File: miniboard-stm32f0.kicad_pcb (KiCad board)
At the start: 2 copper layers, 39.1 x 19.4 mm, 27 parts, among them P1 CONN_01X02, P2 CONN_01X11, P3 CONN_01X01, P4 CONN_02X03, SW1 SW_PUSH, SW2 SW_PUSH, U1 stm32f030f4p6, Y1 8MHz

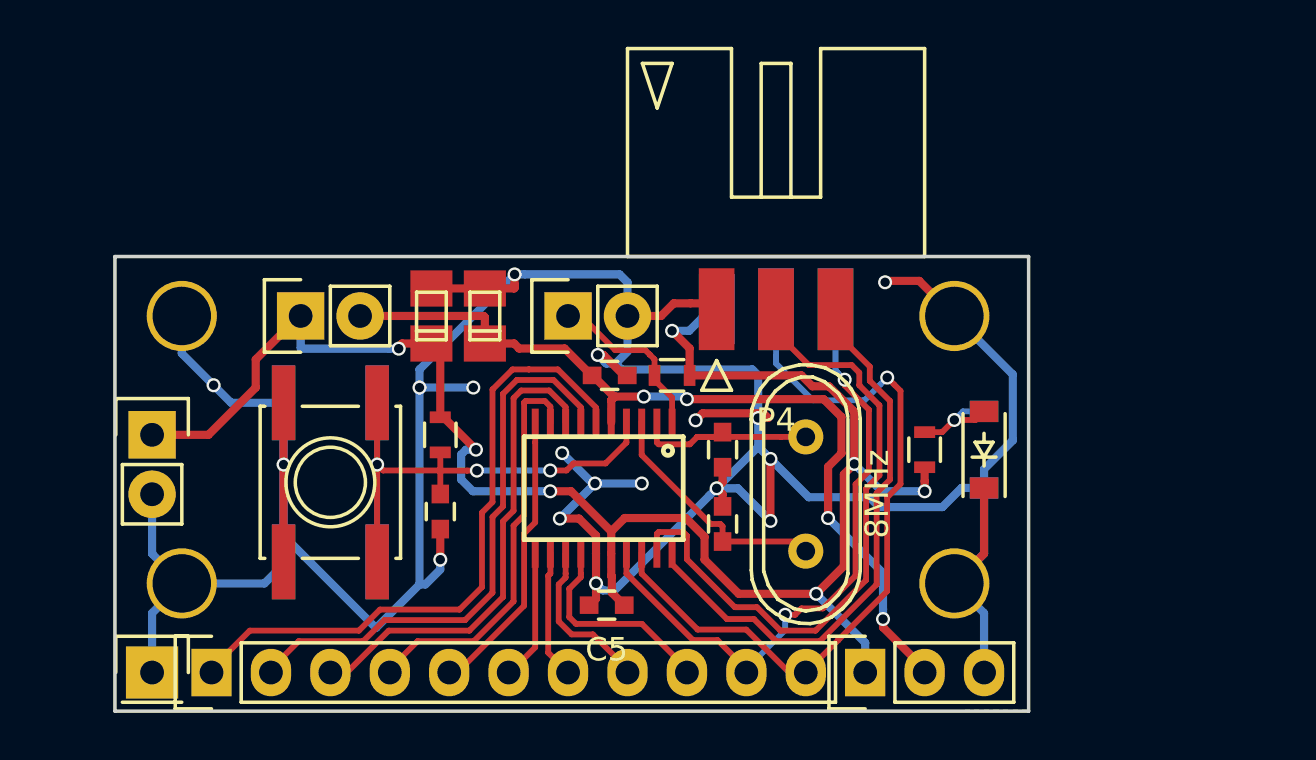
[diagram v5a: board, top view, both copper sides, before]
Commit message: Change direction of power connector
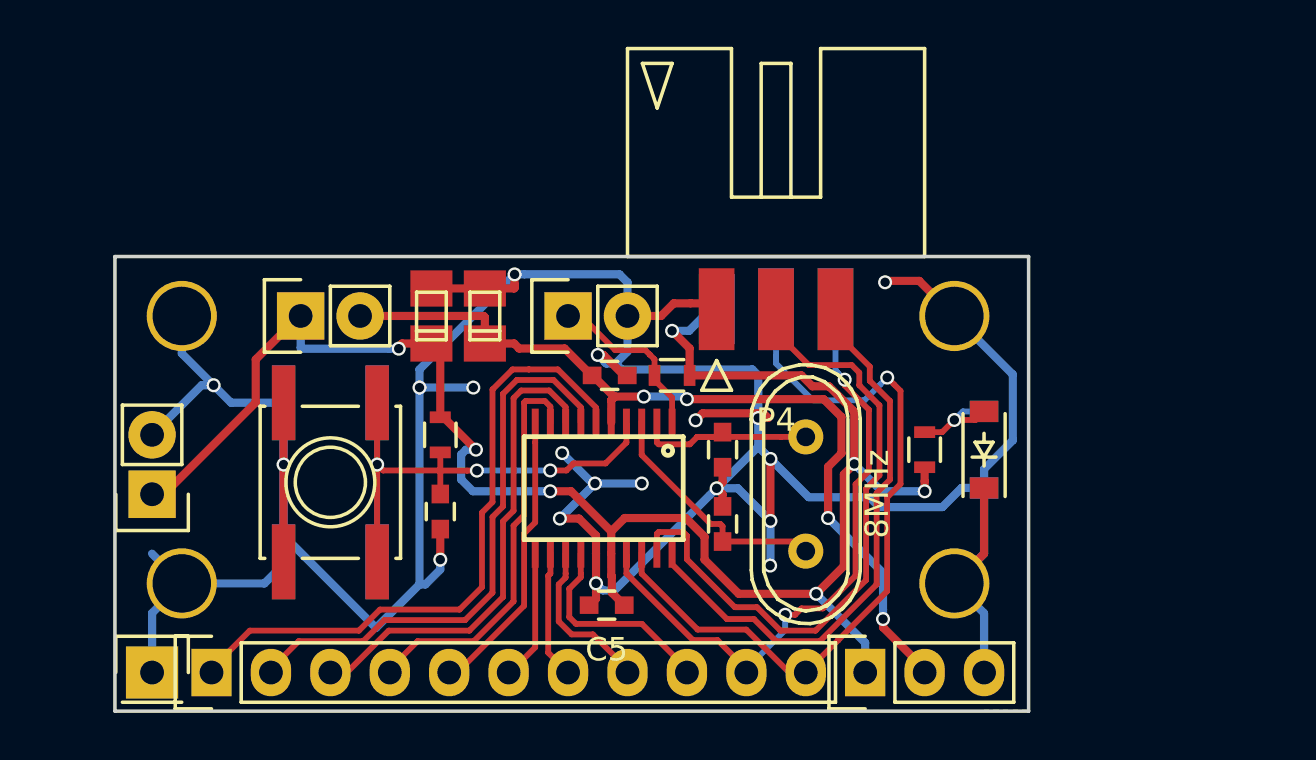
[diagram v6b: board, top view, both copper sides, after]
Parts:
- moved P_POWER1 2.54 mm to (115.6, 111.8), turned to 180 degrees
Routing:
- net GND: track 163.9 -> 166.8 mm, vias 18 -> 19
- net +3V3: track 74.8 -> 76.2 mm
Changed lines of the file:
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@@
     (links 64)
     (no_connects 0)
-    (area 113.907499 101.524999 153.110001 121.106001)
+    (area 110.461667 90.315 154.205 126.393095)
     (thickness 1.6)
-    (drawings 54)
-    (tracks 425)
+    (drawings 57)
+    (tracks 429)
     (zones 0)
     (modules 27)
@@
   )
   (module Pin_Headers:Pin_Header_Straight_1x02 (layer F.Cu)
-    (at 115.57 109.22)
+    (at 115.57 111.76 180)
     (descr "Through hole pin header")
     (tags "pin header")
-    (fp_text reference P_POWER1 (at 0 -5.1) (layer F.SilkS) hide
-      (effects (font (size 1 1) (thickness 0.15)))
-    )
-    (fp_text value CONN_01X02 (at 0 -3.1) (layer F.Fab) hide
+    (fp_text reference P_POWER1 (at 0 -5.1 180) (layer F.SilkS) hide
+      (effects (font (size 1 1) (thickness 0.15)))
+    )
+    (fp_text value CONN_01X02 (at 0 -3.1 180) (layer F.Fab) hide
       (effects (font (size 1 1) (thickness 0.15)))
     )
@@
     (fp_line (start -1.27 1.27) (end -1.27 3.81) (layer F.SilkS) (width 0.15))
     (fp_line (start -1.27 3.81) (end 1.27 3.81) (layer F.SilkS) (width 0.15))
-    (pad 1 thru_hole rect (at 0 0) (size 2.032 2.032) (drill 1.016) (layers *.Cu *.Mask F.SilkS)
+    (pad 1 thru_hole rect (at 0 0 180) (size 2.032 2.032) (drill 1.016) (layers *.Cu *.Mask F.SilkS)
       (net 5 +3V3))
-    (pad 2 thru_hole oval (at 0 2.54) (size 2.032 2.032) (drill 1.016) (layers *.Cu *.Mask F.SilkS)
+    (pad 2 thru_hole oval (at 0 2.54 180) (size 2.032 2.032) (drill 1.016) (layers *.Cu *.Mask F.SilkS)
       (net 2 GND))
     (model Pin_Headers.3dshapes/Pin_Header_Straight_1x02.wrl
@@
       (net 2 GND) (solder_mask_margin 1) (clearance 1))
   )
+  (dimension 50.165 (width 0.3) (layer Dwgs.User)
+    (gr_text "50,165 mm" (at 127.9525 135.335) (layer Dwgs.User)
+      (effects (font (size 1.5 1.5) (thickness 0.3)))
+    )
+    (feature1 (pts (xy 102.87 131.445) (xy 102.87 136.685)))
+    (feature2 (pts (xy 153.035 131.445) (xy 153.035 136.685)))
+    (crossbar (pts (xy 153.035 133.985) (xy 102.87 133.985)))
+    (arrow1a (pts (xy 102.87 133.985) (xy 103.996504 133.398579)))
+    (arrow1b (pts (xy 102.87 133.985) (xy 103.996504 134.571421)))
+    (arrow2a (pts (xy 153.035 133.985) (xy 151.908496 133.398579)))
+    (arrow2b (pts (xy 153.035 133.985) (xy 151.908496 134.571421)))
+  )
+  (dimension 19.685 (width 0.3) (layer Dwgs.User)
+    (gr_text "19,685 mm" (at 160.1 111.4425 90) (layer Dwgs.User)
+      (effects (font (size 1.5 1.5) (thickness 0.3)))
+    )
+    (feature1 (pts (xy 156.21 101.6) (xy 161.45 101.6)))
+    (feature2 (pts (xy 156.21 121.285) (xy 161.45 121.285)))
+    (crossbar (pts (xy 158.75 121.285) (xy 158.75 101.6)))
+    (arrow1a (pts (xy 158.75 101.6) (xy 159.336421 102.726504)))
+    (arrow1b (pts (xy 158.75 101.6) (xy 158.163579 102.726504)))
+    (arrow2a (pts (xy 158.75 121.285) (xy 159.336421 120.158496)))
+    (arrow2b (pts (xy 158.75 121.285) (xy 158.163579 120.158496)))
+  )
+  (dimension 39.37 (width 0.3) (layer Dwgs.User)
+    (gr_text "39,370 mm" (at 133.35 126.445) (layer Dwgs.User)
+      (effects (font (size 1.5 1.5) (thickness 0.3)))
+    )
+    (feature1 (pts (xy 113.665 121.92) (xy 113.665 127.795)))
+    (feature2 (pts (xy 153.035 121.92) (xy 153.035 127.795)))
+    (crossbar (pts (xy 153.035 125.095) (xy 113.665 125.095)))
+    (arrow1a (pts (xy 113.665 125.095) (xy 114.791504 124.508579)))
+    (arrow1b (pts (xy 113.665 125.095) (xy 114.791504 125.681421)))
+    (arrow2a (pts (xy 153.035 125.095) (xy 151.908496 124.508579)))
+    (arrow2b (pts (xy 153.035 125.095) (xy 151.908496 125.681421)))
+  )
   (gr_text RESET (at 127.254 109.22 270) (layer B.SilkS)
     (effects (font (size 1 1) (thickness 0.2)) (justify right mirror))
   )
-  (gr_text SWCLK (at 135.382 109.728 360) (layer B.SilkS)
-    (effects (font (size 1 1) (thickness 0.2)) (justify left mirror))
-  )
-  (gr_text SWDIO (at 135.382 111.76 360) (layer B.SilkS)
-    (effects (font (size 1 1) (thickness 0.2)) (justify left mirror))
-  )
-  (gr_text GND (at 135.382 113.538 360) (layer B.SilkS)
+  (gr_text SWCLK (at 135.382 109.728) (layer B.SilkS)
+    (effects (font (size 1 1) (thickness 0.2)) (justify left mirror))
+  )
+  (gr_text SWDIO (at 135.382 111.76) (layer B.SilkS)
+    (effects (font (size 1 1) (thickness 0.2)) (justify left mirror))
+  )
+  (gr_text GND (at 135.382 113.538) (layer B.SilkS)
     (effects (font (size 1 1) (thickness 0.2)) (justify left mirror))
   )
@@
   (gr_line (start 138.43 114.3) (end 135.636 114.3) (layer B.SilkS) (width 0.2))
   (gr_line (start 138.43 108.966) (end 138.43 114.3) (layer B.SilkS) (width 0.2))
-  (gr_text 3.3 (at 138.684 113.538 360) (layer B.SilkS)
+  (gr_text 3.3 (at 138.684 113.538) (layer B.SilkS)
     (effects (font (size 1 1) (thickness 0.2)) (justify right mirror))
   )
-  (gr_text 3.3V (at 116.84 109.22 360) (layer B.SilkS)
+  (gr_text 3.3V (at 116.84 111.76) (layer B.SilkS)
     (effects (font (size 1 1) (thickness 0.2)) (justify right mirror))
   )
@@
     (effects (font (size 1 1) (thickness 0.2)) (justify right mirror))
   )
-  (gr_text GND (at 118.364 111.76 360) (layer B.SilkS)
+  (gr_text GND (at 118.364 109.22) (layer B.SilkS)
     (effects (font (size 1 1) (thickness 0.2)) (justify mirror))
   )
@@
   (segment (start 137.145 109.55) (end 137.220001 109.625001) (width 0.25) (layer F.Cu) (net 1))
   (segment (start 137.145 108.7) (end 137.145 109.55) (width 0.25) (layer F.Cu) (net 1))
+  (segment (start 142 112.9) (end 142 114.794) (width 0.35) (layer B.Cu) (net 2))
+  (segment (start 142 114.794) (end 141.986 114.808) (width 0.35) (layer B.Cu) (net 2))
+  (via (at 141.986 114.808) (size 0.6) (drill 0.4) (layers F.Cu B.Cu) (net 2))
+  (segment (start 118.2 107.1) (end 117.69 107.1) (width 0.35) (layer B.Cu) (net 2))
+  (segment (start 117.69 107.1) (end 115.57 109.22) (width 0.35) (layer B.Cu) (net 2))
   (segment (start 141.9 108.5) (end 141.700001 108.300001) (width 0.35) (layer F.Cu) (net 2))
   (segment (start 141.700001 108.300001) (end 139.099999 108.300001) (width 0.35) (layer F.Cu) (net 2))
@@
   (segment (start 115.57 119.38) (end 115.57 116.84) (width 0.35) (layer B.Cu) (net 2))
   (segment (start 115.57 116.84) (end 116.84 115.57) (width 0.35) (layer B.Cu) (net 2))
-  (segment (start 115.57 111.76) (end 115.57 114.3) (width 0.35) (layer B.Cu) (net 2))
   (segment (start 115.57 114.3) (end 116.84 115.57) (width 0.35) (layer B.Cu) (net 2))
   (segment (start 121.19 110.49) (end 121.19 114.65) (width 0.35) (layer B.Cu) (net 2))
@@
   (via (at 125.19 110.49) (size 0.6) (drill 0.4) (layers F.Cu B.Cu) (net 4))
   (via (at 132.588 110.744) (size 0.6) (drill 0.4) (layers F.Cu B.Cu) (net 4))
-  (segment (start 115.57 109.22) (end 117.98 109.22) (width 0.35) (layer F.Cu) (net 5))
-  (segment (start 120 107.2) (end 120 106) (width 0.35) (layer F.Cu) (net 5))
-  (segment (start 120 106) (end 121.86 104.14) (width 0.35) (layer F.Cu) (net 5))
-  (segment (start 117.98 109.22) (end 120 107.2) (width 0.35) (layer F.Cu) (net 5))
-  (segment (start 121.86 104.14) (end 121.92 104.14) (width 0.35) (layer F.Cu) (net 5))
+  (segment (start 121.92 104.14) (end 121.86 104.14) (width 0.35) (layer F.Cu) (net 5))
+  (segment (start 121.86 104.14) (end 120 106) (width 0.35) (layer F.Cu) (net 5))
+  (segment (start 120 106) (end 120 107.838) (width 0.35) (layer F.Cu) (net 5))
+  (segment (start 120 107.838) (end 116.078 111.76) (width 0.35) (layer F.Cu) (net 5))
+  (segment (start 116.078 111.76) (end 115.57 111.76) (width 0.35) (layer F.Cu) (net 5))
   (segment (start 145.584011 110.463822) (end 145.137496 110.910337) (width 0.35) (layer F.Cu) (net 5))
   (segment (start 145.137496 110.910337) (end 145.137496 114.831504) (width 0.35) (layer F.Cu) (net 5))

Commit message: Fix footprint for the stm32 and the edge connector
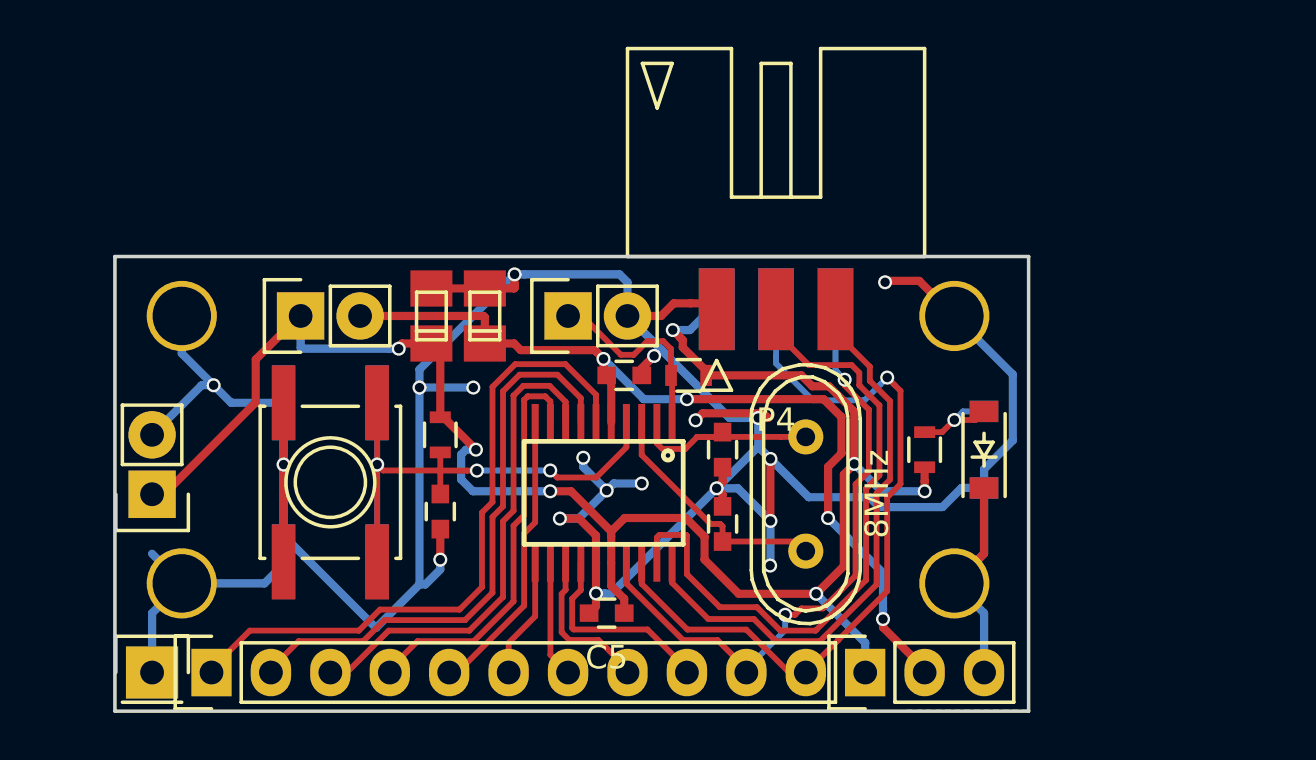
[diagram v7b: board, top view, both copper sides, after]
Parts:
- moved R1 0.71 mm to (138.5, 106.7)
- moved C7 0.62 mm to (135.8, 106.7)
- moved C5 0.34 mm to (135.0, 116.8)
- moved U1 0.20 mm to (134.9, 111.7)
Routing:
- net GND: track 166.8 -> 162.9 mm
- net VAA: track 37.1 -> 38.8 mm
- net /BOOT0: track 7.48 -> 8.64 mm
- net /PA0: track 27.9 -> 28.5 mm
